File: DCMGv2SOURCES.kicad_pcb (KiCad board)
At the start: 2 copper layers, 181 parts, among them P1 24V_IN, P10 NC_SCGR_SIG, P11 IC+OUT, P12 IC-OUT, P13 COIL_OUT, P14 UNREG_V_SIG, P15 UNREG_I_SIG, P16 TO_REG+, P17 TO_REG-, P18 FROM_REG+, P19 FROM_REG-, P2 GND_IN, P20 REG_V_SIG, P21 TO_GRID-, P22 REG_I_SIG, P23 TO_GRID+, P3 FROM_SRC+, P4 CTRL_SIG, P5 FROM_SRC-, P6 GND_IN, P7 IC+IN, P8 IC-IN, P9 COIL+IN, Q1 STS1DNC45, Q2 IRFP260, Q3 STS1DNC45, Q4 IRF5210, Q5 IRF5210, SW1 SPDT_RELAY, SW2 SPDT_RELAY, U1 LT1014DN, U10 LT1634, U11 LT1010, U12 LT1014DN, U13 LT1014DN, U14 ULN2803A, U2 LM339, U3 LT1634, U4 PQMC3-D24-D15, U5 RECOM_R-7XXX, U6 DAUGHTERBOARD_MOUNT, U7 LT1014DN, U8 LT1014DN, U9 LT1014DN

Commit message: thicker traces and vias. some vias still drilled incorrectly
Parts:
- C17, C37: moved to B.Cu
- moved C38 153.0 mm to (150.1, 61.0), turned to 270 degrees
- moved C39 152.5 mm to (156.0, 52.6), turned to 90 degrees
- moved C17 135.9 mm to (131.8, 61.7), turned to 180 degrees
- moved C37 129.8 mm to (132.6, 50.3)
- moved C25 3.45 mm to (166.1, 22.1)
- moved C16 3.31 mm to (121.2, 45.0)
- moved R68 2.84 mm to (158.2, 58.4)
- moved R43 1.30 mm to (159.5, 46.7)
- moved R41 0.76 mm to (160.0, 26.7)
- moved R42 0.76 mm to (166.6, 26.7)
- moved C23 0.51 mm to (64.8, 52.6)
- moved C18 0.51 mm to (63.0, 52.6)
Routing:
- net N-0000020: track 29.4 -> 165.4 mm
- net IC_POW-: track 281.6 -> 334.0 mm
- net IC_POW+: track 387.8 -> 430.3 mm, vias 18 -> 20
- net CTRL_GND: track 96.6 -> 121.4 mm, vias 22 -> 25
- net N-0000028: track 49.9 -> 70.7 mm
- net N-0000058: track 17.8 -> 33.6 mm
- net N-0000051: track 114.6 -> 126.0 mm
- net N-0000060: track 38.0 -> 49.0 mm
- net N-000007: track 54.8 -> 63.6 mm
- net N-0000062: track 53.5 -> 60.5 mm
- net N-0000055: track 21.9 -> 25.9 mm
- net N-0000025: track 0.00 -> 3.09 mm
- net N-0000011: track 5.95 -> 8.48 mm
- net N-0000056: track 196.4 -> 194.0 mm
- net N-0000024: track 16.3 -> 18.3 mm
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
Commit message: split source board into single channel test board and multi channel board with power supply. All vias have been fixed.     NOTE: in the first logged comment, I meant to say that I was working on the SOURCE board.
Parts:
- removed C1: 10u, c_0603
- removed C10, C11, C4, C5, C9: COIL_BYPASS, c_0603
- removed C12, C13, C14: 100u, c_0603
- removed C2, C3: 1u, c_0603
- removed C26, C27, C28, C29, C30, C31, C32: VCC_BYP, c_0603
- removed D2: PDS1040, POWERDI5
- removed P1: 24V_IN, Screw Terminal 8191
- removed P11: IC+OUT, Screw Terminal 8191
- removed P12: IC-OUT, Screw Terminal 8191
- removed P13: COIL_OUT, Screw Terminal 8191
- removed P2: GND_IN, Screw Terminal 8191
- removed R7: 1k, OHMITE_1W
- removed U4: PQMC3-D24-D15, SIL-8 PQMC
- removed U5: RECOM_R-7XXX, R-7xxx_SIL-12
- added R40: MIN_LOAD, c_0805, F.Cu at (230.4, 24.1)
- C15: footprint c_0603 -> c_0805
- C19: moved to F.Cu
- moved C34 282.6 mm to (276.4, 86.9)
- moved C7 116.4 mm to (108.0, 42.7), turned to 180 degrees
- moved P6 99.4 mm to (19.6, 27.9)
- moved P9 99.0 mm to (16.8, 81.8)
- moved P8 95.7 mm to (26.7, 81.8)
- moved P7 95.2 mm to (36.8, 81.8)
- moved C6 83.5 mm to (18.5, 73.4), turned to 180 degrees
- moved C8 83.0 mm to (78.7, 32.5), turned to 270 degrees
- moved P10 14.0 mm to (50.0, 83.8)
- moved P4 11.7 mm to (47.5, 83.8)
- moved R27 5.24 mm to (31.5, 24.9), turned to 90 degrees
- moved R55 5.14 mm to (170.9, 46.2), turned to 270 degrees
- moved P18 4.19 mm to (222.0, 25.1)
- moved R57 3.88 mm to (224.0, 66.3)
- moved C44 2.65 mm to (168.7, 46.2), turned to 270 degrees
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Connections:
- SW1 pad 2: N-0000020 (its old number) -> COIL_POW+
- SW2 pad 2: N-0000020 (its old number) -> COIL_POW+
- U14 pad 10: (no net) -> COIL_POW+
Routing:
- net COIL_POW+: track 0.00 -> 208.0 mm, vias 0 -> 1
- net N-0000020 (its old number): track 165.4 -> 0.00 mm
- net CTRL_GND: track 121.4 -> 147.9 mm, vias 25 -> 30
- net IC_POW-: track 334.0 -> 348.4 mm
- net N-0000051: track 89.3 -> 75.3 mm
- net N-0000021: track 70.7 -> 82.5 mm
- net N-0000071: track 141.2 -> 151.6 mm
- net N-0000049: track 88.0 -> 78.7 mm
- net N-0000027: track 25.6 -> 34.0 mm
- net IC_POW+: track 430.3 -> 434.8 mm
- net N-0000017: track 18.3 -> 14.6 mm
- net N-0000039: track 20.7 -> 24.0 mm
- net N-0000019: track 21.6 -> 24.4 mm
- net N-0000044: track 93.6 -> 95.8 mm
- net N-0000025: track 15.8 -> 13.7 mm
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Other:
- board outline added: 262.4 x 71.6 mm
- board text added: "SOURCE TEST BOARD - JORDAN MURRAY - FEB 2016"

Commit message: added power indicators. added mounting holes. board size increased slightly in y dim. fixed important schematic and routing error involving U8B and U8D!
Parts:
- added 3mm_hole: VAL**, 3mm_hole, F.Cu at (41.9, 51.6)
- added 3mm_hole: VAL**, 3mm_hole, F.Cu at (270.3, 84.1)
- added 3mm_hole: VAL**, 3mm_hole, F.Cu at (270.5, 19.8)
- added 3mm_hole: VAL**, 3mm_hole, F.Cu at (168.1, 80.3)
- added D11: LED_RED, 1209, F.Cu at (28.4, 86.1)
- added D12: LED_RED, 1209, F.Cu at (18.3, 86.1)
- added D2: LED_RED, 1209, F.Cu at (42.2, 86.1)
- added R10: 2.2k, c_0805, F.Cu at (22.6, 86.1)
- added R6: 2.2k, c_0805, F.Cu at (38.1, 86.1)
- added R7: 2.2k, c_0805, F.Cu at (32.8, 86.1)
- R78, R79, R80, R81: footprint c_0603 -> c_0805
- moved C34 252.4 mm to (24.4, 72.9), turned to 180 degrees
- moved R31 16.3 mm to (56.6, 69.8), turned to 270 degrees
- moved R29 15.7 mm to (62.7, 75.4), turned to 0 degrees
- moved R32 15.4 mm to (72.9, 63.0), turned to 270 degrees
- moved R34 12.3 mm to (71.1, 63.0), turned to 90 degrees
- moved R35 6.36 mm to (62.2, 73.7), turned to 180 degrees
- moved C21 3.97 mm to (67.1, 67.8), turned to 270 degrees
- moved P10 3.88 mm to (53.3, 85.9)
- moved P4 3.88 mm to (50.8, 85.9)
- moved D5 3.82 mm to (75.4, 67.6)
- moved R30 2.30 mm to (71.1, 66.3), turned to 90 degrees
- moved P7 2.27 mm to (38.9, 80.8)
- moved C41 2.17 mm to (60.5, 65.0), turned to 0 degrees
- moved R80 2.09 mm to (73.7, 71.9)
- moved R60 1.78 mm to (151.6, 43.9)
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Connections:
- R29 pad 2: N-0000083 (its old number) -> N-0000084
- R31 pad 1: N-0000083 (its old number) -> N-0000084
- R32 pad 2: N-0000085 (its old number) -> N-0000082
- R34 pad 1: N-0000085 (its old number) -> N-0000082
- U8 pad 16: (no net) -> N-0000082
- U8 pad 7: (no net) -> N-0000084
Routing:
- net N-0000083: track 24.9 -> 9.11 mm
- net CTRL_GND: track 147.9 -> 159.0 mm, vias 30 -> 32
- net N-0000084: track 0.00 -> 10.9 mm
- net IC_POW-: track 348.4 -> 358.8 mm, vias 15 -> 13
- net N-0000085: track 26.8 -> 18.5 mm
- net IC_POW+: track 434.8 -> 441.8 mm, vias 20 -> 19
- net N-0000083 (its old number): track 5.31 -> 0.00 mm
- net N-0000031: track 78.7 -> 73.8 mm
- net N-0000082: track 0.00 -> 4.23 mm
- net N-0000028: track 75.3 -> 71.1 mm
- net N-0000048: track 12.7 -> 8.92 mm
- net N-0000011: track 63.6 -> 66.9 mm
- net N-0000094: track 0.00 -> 3.16 mm
- net N-0000093: track 0.00 -> 3.16 mm
- net N-0000096: track 0.00 -> 2.91 mm
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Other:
- board size 262.4 x 71.6 mm -> 262.4 x 74.2 mm

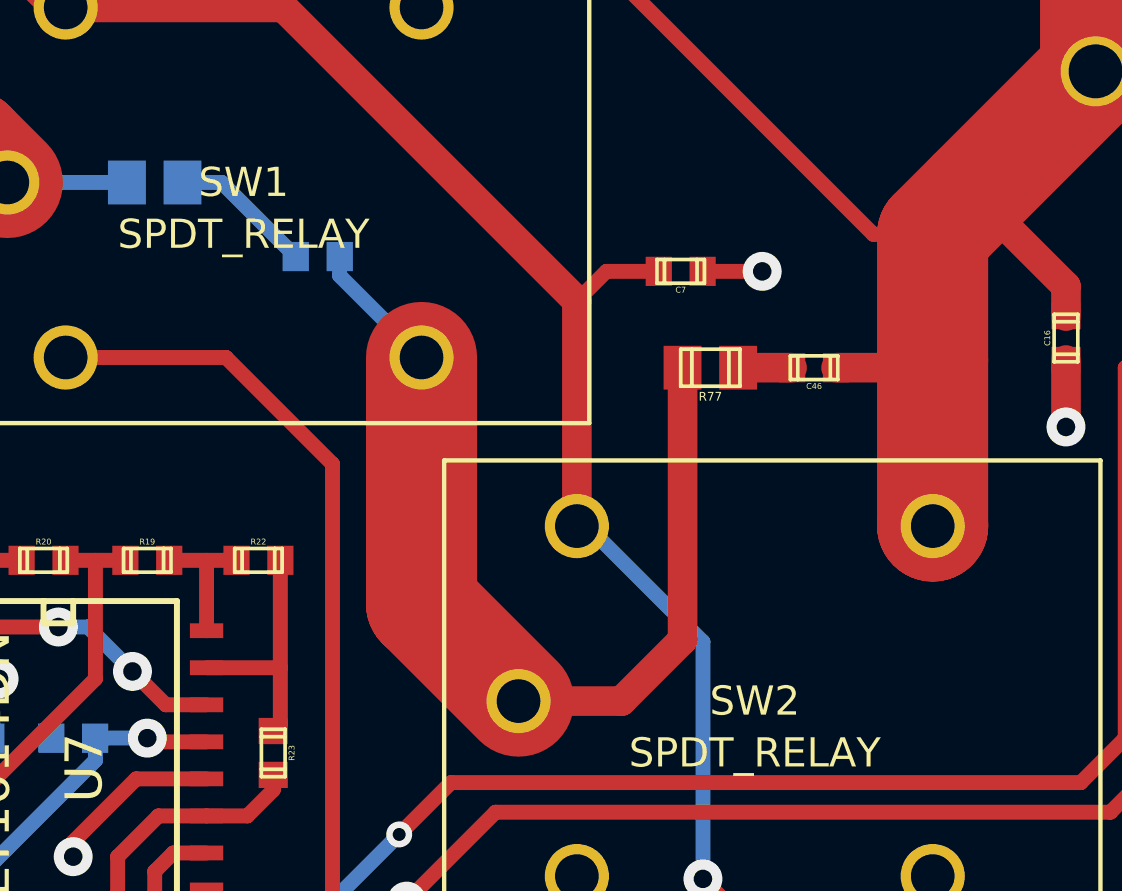
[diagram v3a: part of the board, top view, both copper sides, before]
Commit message: snubber capacitors now 0805
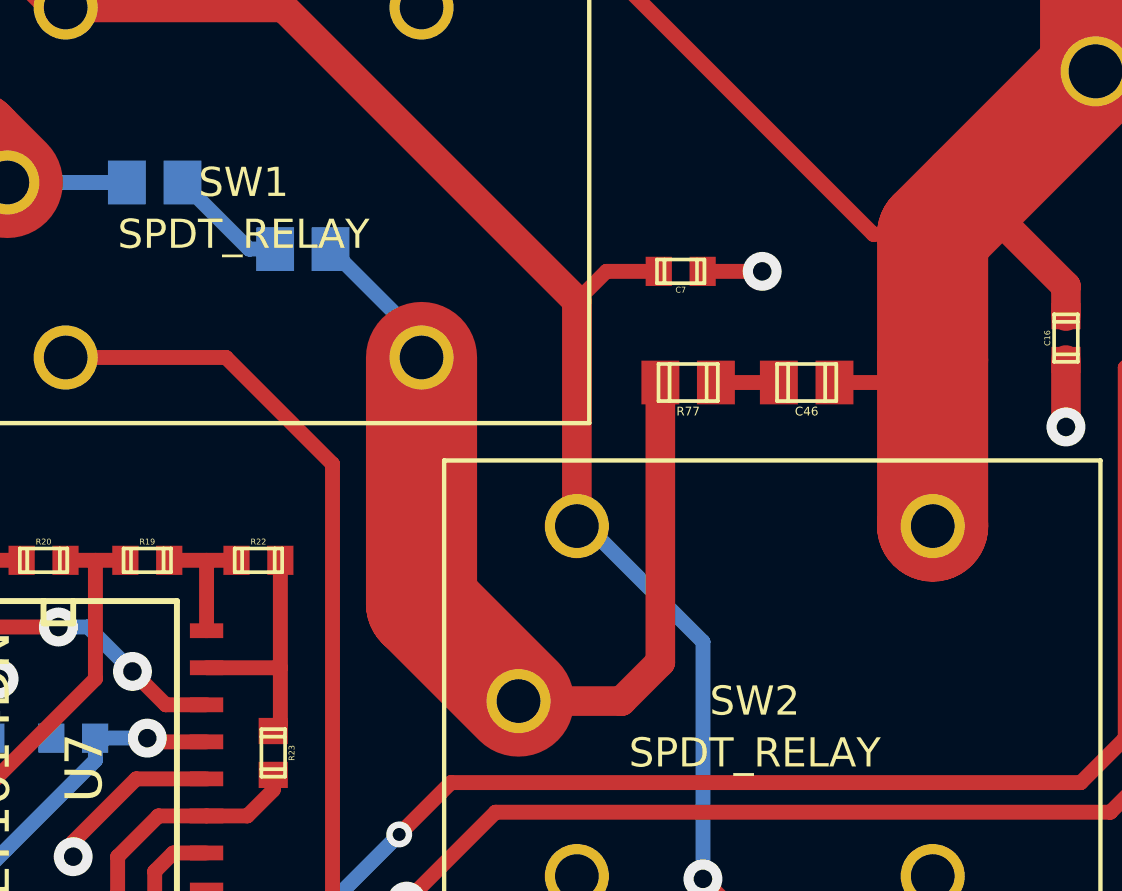
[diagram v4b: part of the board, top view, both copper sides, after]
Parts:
- C45, C46: footprint c_0603 -> c_0805
- moved R77 0.92 mm to (108.2, 46.5)
- moved C45 0.57 mm to (95.0, 41.9)
- moved C46 0.57 mm to (112.3, 46.5)
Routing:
- net N-0000026: track 4.94 -> 4.12 mm
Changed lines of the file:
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@@
     (links 332)
     (no_connects 22)
-    (area 13.919999 15.189999 276.402001 86.918001)
+    (area 13.919999 15.189999 276.402001 89.458001)
     (thickness 1.6)
     (drawings 6)
-    (tracks 1149)
+    (tracks 1150)
     (zones 0)
     (modules 165)
@@
     (add_net N-0000017)
     (add_net N-0000020)
-    (add_net N-0000025)
     (add_net N-0000027)
     (add_net N-0000029)
@@
     (add_net N-0000023)
     (add_net N-0000024)
+    (add_net N-0000025)
+    (add_net N-0000026)
     (add_net N-0000028)
     (add_net N-000003)
@@
     (uvia_dia 0.508)
     (uvia_drill 0.127)
-    (add_net N-0000026)
   )
   (net_class ic_power ""
@@
   )
   (module c_0805 (layer F.Cu)
-    (at 108.966 45.974 180)
+    (at 108.204 46.482 180)
     (descr "SMT capacitor, 0805")
     (fp_text reference R77 (at 0 -0.9906 180) (layer F.SilkS)
@@
     )
   )
-  (module c_0603 (layer B.Cu)
-    (at 95.504 42.164 180)
-    (descr "SMT capacitor, 0603")
-    (fp_text reference C45 (at 0 0.635 180) (layer B.SilkS)
-      (effects (font (size 0.20066 0.20066) (thickness 0.04064)) (justify mirror))
-    )
-    (fp_text value C (at 0 -0.635 180) (layer B.SilkS) hide
-      (effects (font (size 0.20066 0.20066) (thickness 0.04064)) (justify mirror))
-    )
-    (fp_line (start 0.5588 -0.4064) (end 0.5588 0.4064) (layer B.SilkS) (width 0.127))
-    (fp_line (start -0.5588 0.381) (end -0.5588 -0.4064) (layer B.SilkS) (width 0.127))
-    (fp_line (start -0.8128 0.4064) (end 0.8128 0.4064) (layer B.SilkS) (width 0.127))
-    (fp_line (start 0.8128 0.4064) (end 0.8128 -0.4064) (layer B.SilkS) (width 0.127))
-    (fp_line (start 0.8128 -0.4064) (end -0.8128 -0.4064) (layer B.SilkS) (width 0.127))
-    (fp_line (start -0.8128 -0.4064) (end -0.8128 0.4064) (layer B.SilkS) (width 0.127))
-    (pad 1 smd rect (at 0.75184 0 180) (size 0.89916 1.00076)
-      (layers B.Cu B.Paste B.Mask)
-      (net 26 N-0000026)
-    )
-    (pad 2 smd rect (at -0.75184 0 180) (size 0.89916 1.00076)
-      (layers B.Cu B.Paste B.Mask)
-      (net 24 N-0000024)
-    )
-    (model smd/capacitors/c_0603.wrl
-      (at (xyz 0 0 0))
-      (scale (xyz 1 1 1))
-      (rotate (xyz 0 0 0))
-    )
-  )
-  (module c_0603 (layer F.Cu)
-    (at 112.522 45.974 180)
-    (descr "SMT capacitor, 0603")
-    (fp_text reference C46 (at 0 -0.635 180) (layer F.SilkS)
-      (effects (font (size 0.20066 0.20066) (thickness 0.04064)))
-    )
-    (fp_text value C (at 0 0.635 180) (layer F.SilkS) hide
-      (effects (font (size 0.20066 0.20066) (thickness 0.04064)))
-    )
-    (fp_line (start 0.5588 0.4064) (end 0.5588 -0.4064) (layer F.SilkS) (width 0.127))
-    (fp_line (start -0.5588 -0.381) (end -0.5588 0.4064) (layer F.SilkS) (width 0.127))
-    (fp_line (start -0.8128 -0.4064) (end 0.8128 -0.4064) (layer F.SilkS) (width 0.127))
-    (fp_line (start 0.8128 -0.4064) (end 0.8128 0.4064) (layer F.SilkS) (width 0.127))
-    (fp_line (start 0.8128 0.4064) (end -0.8128 0.4064) (layer F.SilkS) (width 0.127))
-    (fp_line (start -0.8128 0.4064) (end -0.8128 -0.4064) (layer F.SilkS) (width 0.127))
-    (pad 1 smd rect (at 0.75184 0 180) (size 0.89916 1.00076)
-      (layers F.Cu F.Paste F.Mask)
-      (net 25 N-0000025)
-    )
-    (pad 2 smd rect (at -0.75184 0 180) (size 0.89916 1.00076)
-      (layers F.Cu F.Paste F.Mask)
-      (net 33 N-0000032)
-    )
-    (model smd/capacitors/c_0603.wrl
-      (at (xyz 0 0 0))
-      (scale (xyz 1 1 1))
-      (rotate (xyz 0 0 0))
-    )
-  )
   (module Bourns_3361 (layer F.Cu)
     (at 76.962 46.228 180)
@@
     )
   )
+  (module c_0805 (layer F.Cu)
+    (at 112.268 46.482 180)
+    (descr "SMT capacitor, 0805")
+    (fp_text reference C46 (at 0 -0.9906 180) (layer F.SilkS)
+      (effects (font (size 0.29972 0.29972) (thickness 0.06096)))
+    )
+    (fp_text value C (at 0 0.9906 180) (layer F.SilkS) hide
+      (effects (font (size 0.29972 0.29972) (thickness 0.06096)))
+    )
+    (fp_line (start 0.635 -0.635) (end 0.635 0.635) (layer F.SilkS) (width 0.127))
+    (fp_line (start -0.635 -0.635) (end -0.635 0.6096) (layer F.SilkS) (width 0.127))
+    (fp_line (start -1.016 -0.635) (end 1.016 -0.635) (layer F.SilkS) (width 0.127))
+    (fp_line (start 1.016 -0.635) (end 1.016 0.635) (layer F.SilkS) (width 0.127))
+    (fp_line (start 1.016 0.635) (end -1.016 0.635) (layer F.SilkS) (width 0.127))
+    (fp_line (start -1.016 0.635) (end -1.016 -0.635) (layer F.SilkS) (width 0.127))
+    (pad 1 smd rect (at 0.9525 0 180) (size 1.30048 1.4986)
+      (layers F.Cu F.Paste F.Mask)
+      (net 25 N-0000025)
+    )
+    (pad 2 smd rect (at -0.9525 0 180) (size 1.30048 1.4986)
+      (layers F.Cu F.Paste F.Mask)
+      (net 33 N-0000032)
+    )
+    (model smd/capacitors/c_0805.wrl
+      (at (xyz 0 0 0))
+      (scale (xyz 1 1 1))
+      (rotate (xyz 0 0 0))
+    )
+  )
+  (module c_0805 (layer B.Cu)
+    (at 94.996 41.91 180)
+    (descr "SMT capacitor, 0805")
+    (fp_text reference C45 (at 0 0.9906 180) (layer B.SilkS)
+      (effects (font (size 0.29972 0.29972) (thickness 0.06096)) (justify mirror))
+    )
+    (fp_text value C (at 0 -0.9906 180) (layer B.SilkS) hide
+      (effects (font (size 0.29972 0.29972) (thickness 0.06096)) (justify mirror))
+    )
+    (fp_line (start 0.635 0.635) (end 0.635 -0.635) (layer B.SilkS) (width 0.127))
+    (fp_line (start -0.635 0.635) (end -0.635 -0.6096) (layer B.SilkS) (width 0.127))
+    (fp_line (start -1.016 0.635) (end 1.016 0.635) (layer B.SilkS) (width 0.127))
+    (fp_line (start 1.016 0.635) (end 1.016 -0.635) (layer B.SilkS) (width 0.127))
+    (fp_line (start 1.016 -0.635) (end -1.016 -0.635) (layer B.SilkS) (width 0.127))
+    (fp_line (start -1.016 -0.635) (end -1.016 0.635) (layer B.SilkS) (width 0.127))
+    (pad 1 smd rect (at 0.9525 0 180) (size 1.30048 1.4986)
+      (layers B.Cu B.Paste B.Mask)
+      (net 26 N-0000026)
+    )
+    (pad 2 smd rect (at -0.9525 0 180) (size 1.30048 1.4986)
+      (layers B.Cu B.Paste B.Mask)
+      (net 24 N-0000024)
+    )
+    (model smd/capacitors/c_0805.wrl
+      (at (xyz 0 0 0))
+      (scale (xyz 1 1 1))
+      (rotate (xyz 0 0 0))
+    )
+  )
   (gr_line (start 276.352 89.408) (end 276.352 15.24) (angle 90) (layer Edge.Cuts) (width 0.1))
   (gr_line (start 13.97 89.408) (end 276.352 89.408) (angle 90) (layer Edge.Cuts) (width 0.1))
@@
   (segment (start 91.694 62.611) (end 90.551 62.611) (width 0.512) (layer F.Cu) (net 23))
   (segment (start 90.551 62.611) (end 89.916 63.246) (width 0.512) (layer F.Cu) (net 23))
-  (segment (start 108.0135 45.974) (end 108.0135 55.3085) (width 1.016) (layer F.Cu) (net 24))
+  (segment (start 99.064 45.624) (end 99.064 45.0255) (width 0.512) (layer B.Cu) (net 24))
+  (segment (start 99.064 45.0255) (end 95.9485 41.91) (width 0.512) (layer B.Cu) (net 24))
+  (segment (start 107.2515 46.482) (end 107.2515 56.0705) (width 1.016) (layer F.Cu) (net 24))
   (segment (start 105.918 57.404) (end 102.39 57.404) (width 1.016) (layer F.Cu) (net 24))
-  (segment (start 108.0135 55.3085) (end 105.918 57.404) (width 1.016) (layer F.Cu) (net 24))
+  (segment (start 107.2515 56.0705) (end 105.918 57.404) (width 1.016) (layer F.Cu) (net 24))
   (segment (start 99.064 45.624) (end 99.064 54.078) (width 3.81) (layer F.Cu) (net 24))
   (segment (start 99.064 54.078) (end 102.39 57.404) (width 3.81) (layer F.Cu) (net 24))
-  (segment (start 96.25584 42.164) (end 96.25584 42.81584) (width 0.512) (layer B.Cu) (net 24))
-  (segment (start 96.25584 42.81584) (end 99.064 45.624) (width 0.512) (layer B.Cu) (net 24))
-  (segment (start 109.9185 45.974) (end 111.77016 45.974) (width 1.016) (layer F.Cu) (net 25))
-  (segment (start 90.8685 39.624) (end 92.21216 39.624) (width 0.512) (layer B.Cu) (net 26))
-  (segment (start 92.21216 39.624) (end 94.75216 42.164) (width 0.512) (layer B.Cu) (net 26))
+  (segment (start 109.1565 46.482) (end 111.3155 46.482) (width 0.512) (layer F.Cu) (net 25))
+  (segment (start 94.0435 41.91) (end 93.1545 41.91) (width 0.512) (layer B.Cu) (net 26))
+  (segment (start 93.1545 41.91) (end 90.8685 39.624) (width 0.512) (layer B.Cu) (net 26))
   (segment (start 140.72616 40.894) (end 139.7 40.894) (width 0.512) (layer F.Cu) (net 27))
   (segment (start 139.446 41.148) (end 139.446 42.926) (width 0.512) (layer F.Cu) (net 27))
@@
   (segment (start 119.38 84.328) (end 118.872 84.836) (width 0.254) (layer F.Cu) (net 32))
   (segment (start 119.38 82.804) (end 119.38 81.28) (width 0.254) (layer F.Cu) (net 32))
+  (segment (start 113.2205 46.482) (end 115.824 46.482) (width 0.512) (layer F.Cu) (net 33))
+  (segment (start 115.824 46.482) (end 116.586 45.72) (width 0.512) (layer F.Cu) (net 33))
   (segment (start 60.071 22.987) (end 42.037 22.987) (width 0.512) (layer F.Cu) (net 33))
   (segment (start 42.037 22.987) (end 38.1 26.924) (width 0.512) (layer F.Cu) (net 33))
   (segment (start 121.158 44.20616) (end 121.158 43.18) (width 1.016) (layer F.Cu) (net 33) (status 10))
   (segment (start 121.158 43.18) (end 117.983 40.005) (width 1.016) (layer F.Cu) (net 33))
-  (segment (start 113.27384 45.974) (end 116.586 45.974) (width 1.016) (layer F.Cu) (net 33))
   (segment (start 116.586 45.974) (end 116.586 45.72) (width 1.016) (layer F.Cu) (net 33))
   (segment (start 122.174 35.814) (end 122.174 30.814) (width 3.81) (layer F.Cu) (net 33))

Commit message: added labels and made IC power traces thicker
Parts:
- moved Q4 4.06 mm to (175.3, 24.1)
- moved P4 2.79 mm to (53.6, 85.9)
- moved P10 2.29 mm to (51.1, 85.9)
- moved Q5 1.27 mm to (193.8, 24.1)
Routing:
- net IC_POW-: track 358.8 -> 311.6 mm
- net N-0000011: track 66.9 -> 57.2 mm
- net N-0000050: track 14.6 -> 20.0 mm
- net IC_POW+: track 441.8 -> 446.6 mm
- net N-0000028: track 71.1 -> 75.9 mm
- net N-0000059: track 82.2 -> 77.7 mm
- net N-0000031: track 73.8 -> 69.5 mm
- net N-0000043: track 195.4 -> 192.1 mm
- net N-0000052: track 34.0 -> 32.7 mm
- net N-0000075: track 181.1 -> 181.9 mm
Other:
- board text added: "+12V"
- board text added: "+15V"
- board text added: "-15V"
- board text added: "GND"
- board text added: "GND IN"
- board text added: "I lim adj"
- board text added: "Imax!"
- board text added: "Input Status"
- board text added: "Ireg"
- board text added: "Irev!"
- board text added: "Iunreg"
- board text added: "Output Status"
- board text added: "SG"
- board text added: "SINGLE CH SOURCE BOARD v1.0 JORDAN MURRAY - jmm72@case.edu MAR 2016"
- board text added: "Unreg V+"
- board text added: "Unreg V-"
- board text added: "V lim adj"
- board text added: "Vmax!"
- board text added: "Vreg"
- board text added: "Vunreg"
- board text added: "reg V"
- board text added: "user"
- board text removed: "SOURCE TEST BOARD - JORDAN MURRAY - FEB 2016"

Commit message: shortened board in X direction and remade fab files
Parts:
- moved P21 9.91 mm to (248.9, 55.6)
- moved P23 9.86 mm to (249.2, 34.0)
- moved 3mm_hole 8.65 mm to (261.9, 20.3)
- moved 3mm_hole 8.44 mm to (261.9, 83.1)
- moved R64 2.75 mm to (244.1, 29.7), turned to 270 degrees
- moved D9 1.30 mm to (251.5, 42.2)
- moved R62 1.27 mm to (251.5, 47.5)
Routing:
- net N-000006: track 151.6 -> 157.0 mm
- net CTRL_GND: track 159.0 -> 156.6 mm
- net N-0000072: track 160.6 -> 158.5 mm
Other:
- board size 262.4 x 74.2 mm -> 253 x 74.2 mm
